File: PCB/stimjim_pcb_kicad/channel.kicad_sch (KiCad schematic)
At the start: 66 parts, among them J8 Screw_Terminal_01x02, J9 Conn_Coaxial, U13 CC3-0512DF-E, U14 ISO7760, U15 ISO7741, U16 L78L05_SO8, U17 AD5752, U18 AD7321, U19 AD1582, U20 OPA197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

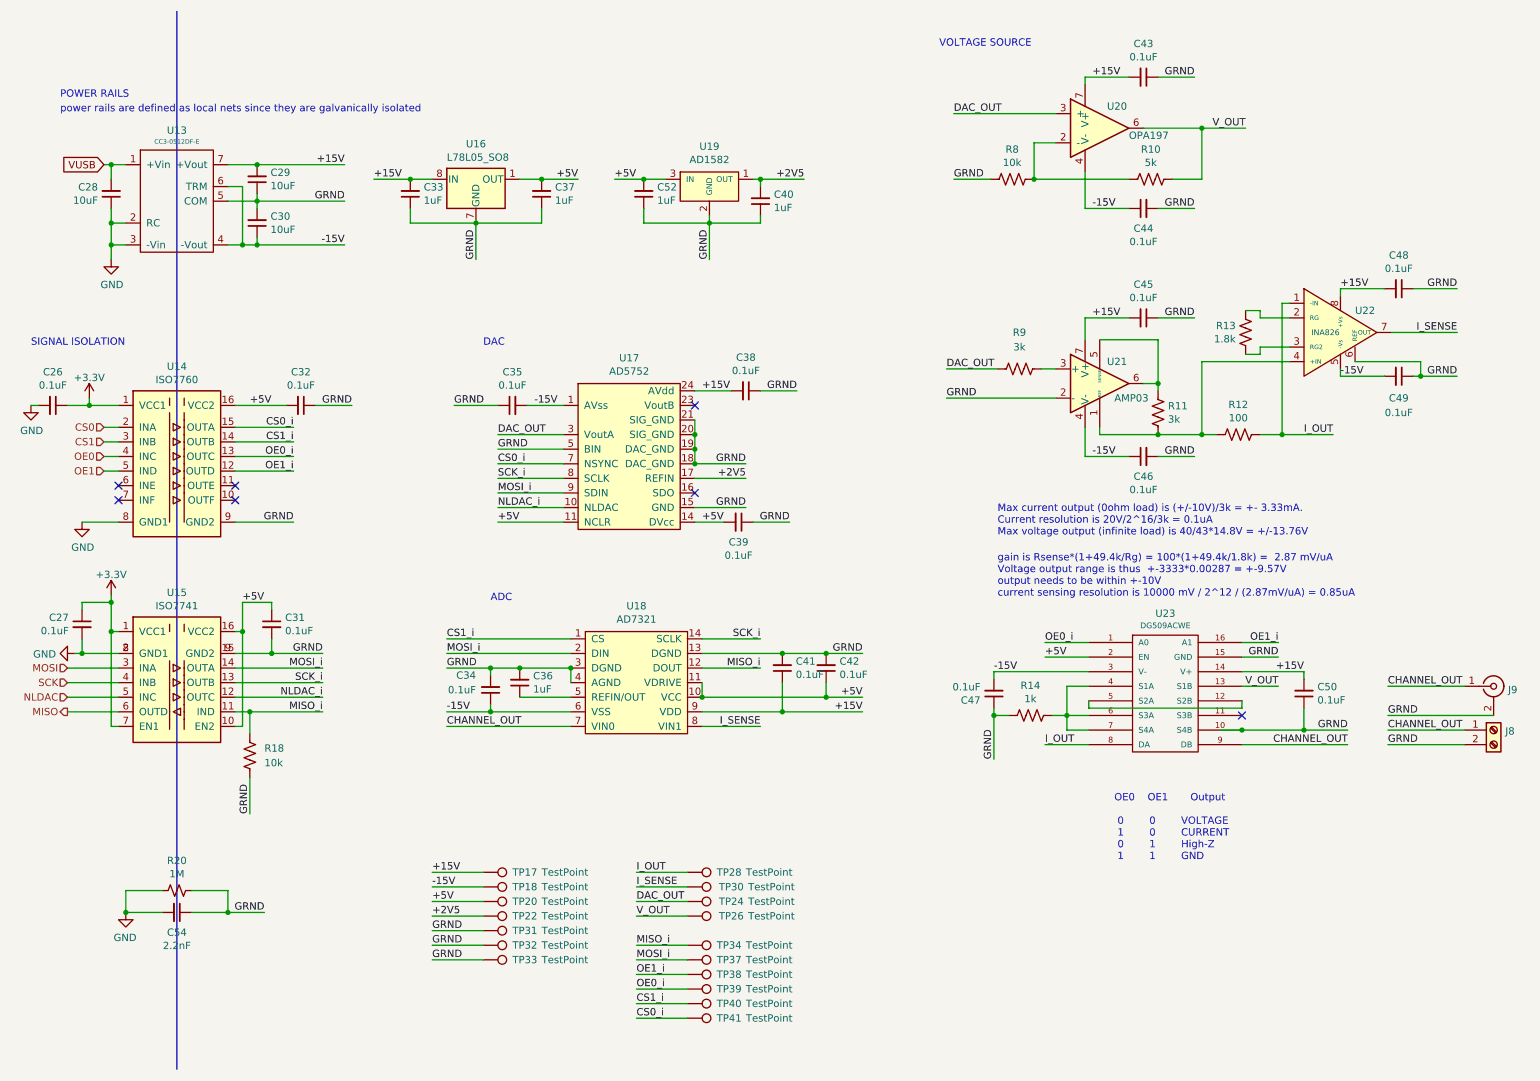
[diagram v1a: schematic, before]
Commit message: Replace teensy with RP235xB
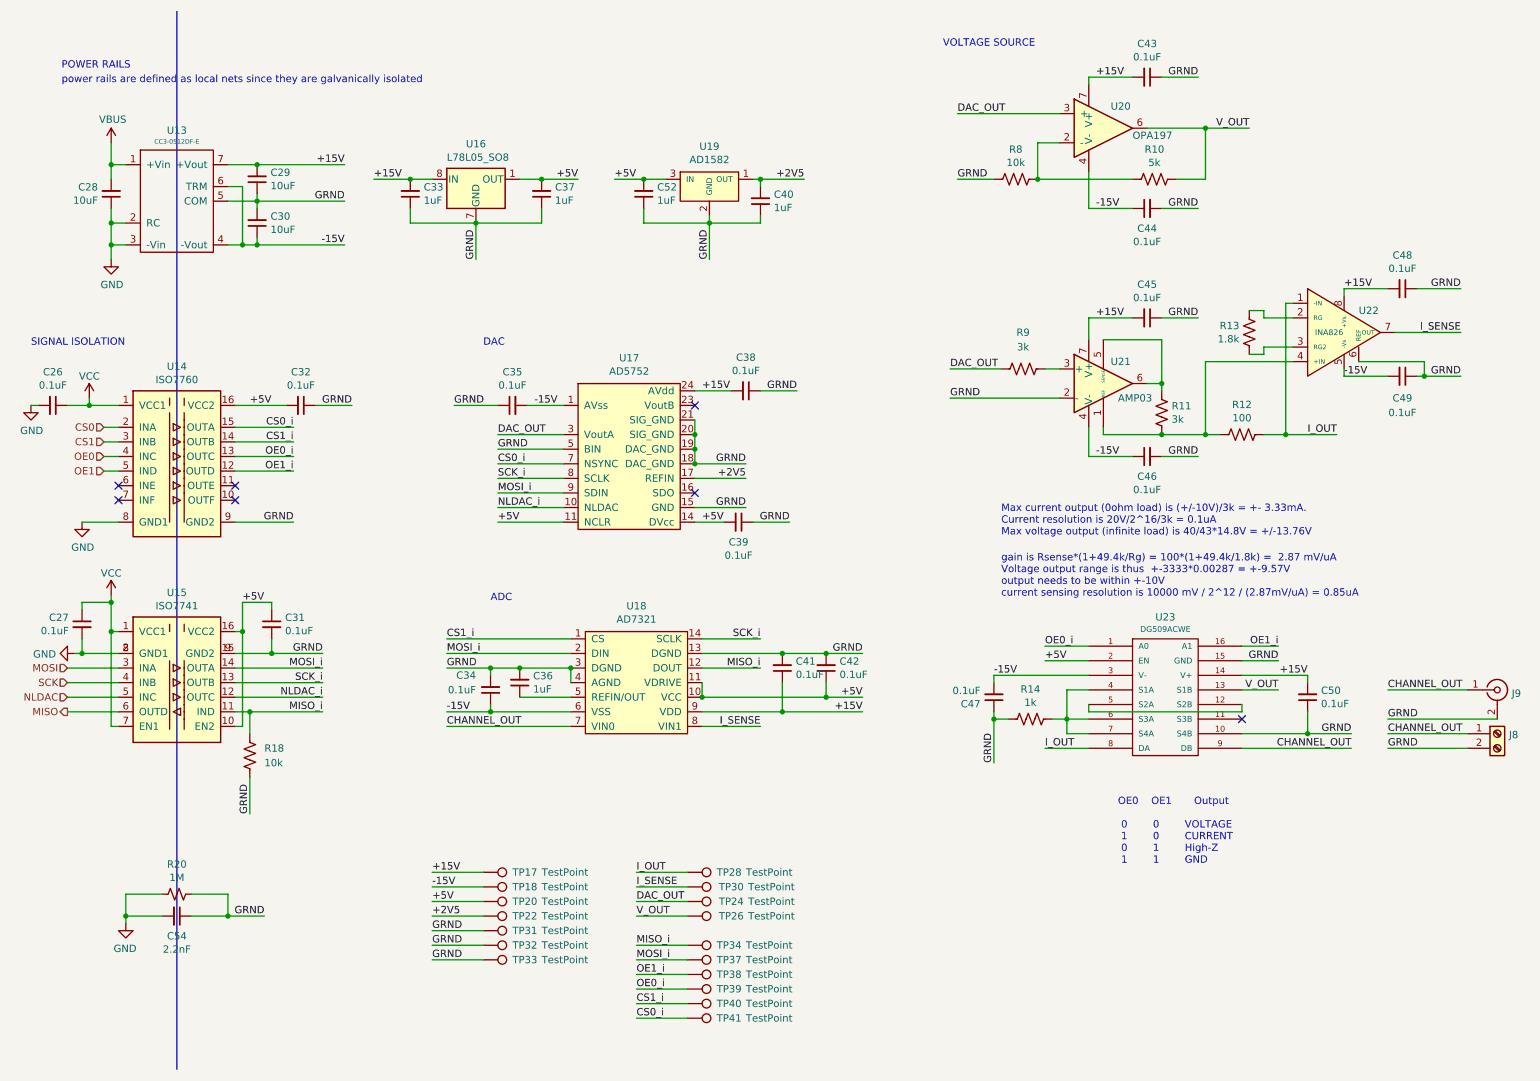
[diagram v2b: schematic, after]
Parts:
- TP17, TP18, TP20, TP22, TP24, TP26, TP28, TP30, TP31, TP32, TP33, TP34, TP37, TP38, TP39, TP40, TP41: now left out of the parts list
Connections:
- net +3.3V renamed VCC
- net VUSB renamed VBUS
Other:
- moved on the sheet: C43, C44, C45, C46, C47, C48, C49, C50, C54, J8, J9, R10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

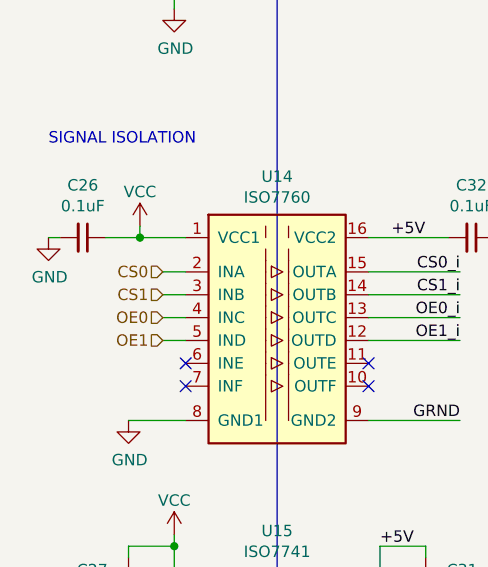
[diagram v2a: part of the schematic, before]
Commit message: Simplified layout
- Went to 4 layers
- Simplified GPIO interface and remove power connections since they are
  a recipe for disaster
- Independent SPI busses to each stimulator to allow simultaneous
  control
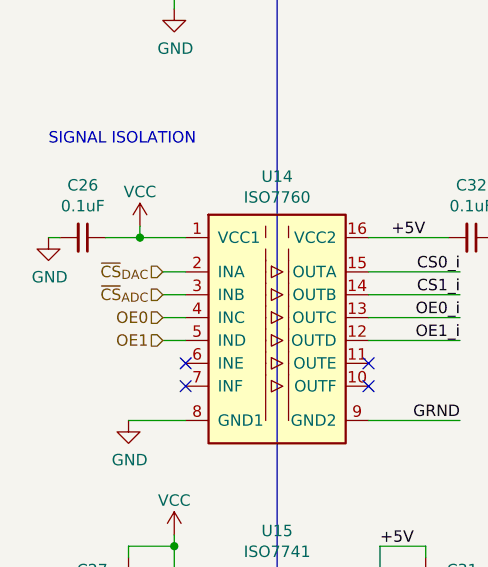
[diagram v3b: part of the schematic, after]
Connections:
- net CS0 renamed ~{CS}_{DAC}
- net CS1 renamed ~{CS}_{ADC}
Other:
- title: (none) -> StimJim
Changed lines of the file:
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@@
 	(generator_version "9.0")
 	(paper "A4")
+	(title_block
+		(title "StimJim")
+		(rev "B")
+		(comment 1 "Nate Cermak")
+		(comment 2 "Jonathan Newman")
+		(comment 3 "Cris Sharp")
+	)
 	(text "power rails are defined as local nets since they are galvanically isolated"
 		(exclude_from_sim no)
@@
 		)
 	)
-	(hierarchical_label "CS0"
+	(hierarchical_label "~{CS}_{DAC}"
 		(shape input)
 		(at 35.56 85.09 180)
@@
 		)
 	)
-	(hierarchical_label "CS1"
+	(hierarchical_label "~{CS}_{ADC}"
 		(shape input)
 		(at 35.56 87.63 180)

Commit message: filipe feedback
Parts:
- J9: footprint microstim:731375003 -> Connector_Coaxial:BNC_Amphenol_B6252HB-NPP3G-50_Horizontal
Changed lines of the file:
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@@
 			)
 		)
-		(property "Footprint" "microstim:731375003"
+		(property "Footprint" "Connector_Coaxial:BNC_Amphenol_B6252HB-NPP3G-50_Horizontal"
 			(at 278.13 130.81 0)
 			(effects
